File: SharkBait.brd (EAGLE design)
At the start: 50 x 92.4 mm, 37 parts, among them J1 BC501SM-TR, Q1 L78M05CDT, U2 DS3231M+

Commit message: brd version 1
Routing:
- net GND: track 378.1 -> 546.9 mm, vias 3 -> 8
- net A0: track 0.00 -> 114.6 mm, vias 0 -> 2
- net A1: track 0.00 -> 90.6 mm, vias 0 -> 1
- net 5V: track 190.3 -> 272.6 mm, vias 1 -> 5
- net D7: track 0.43 -> 76.5 mm, vias 0 -> 1
- net D4: track 0.00 -> 48.4 mm
- net RST: track 2.38 -> 30.7 mm, vias 0 -> 2
- net D5: track 34.1 -> 32.4 mm

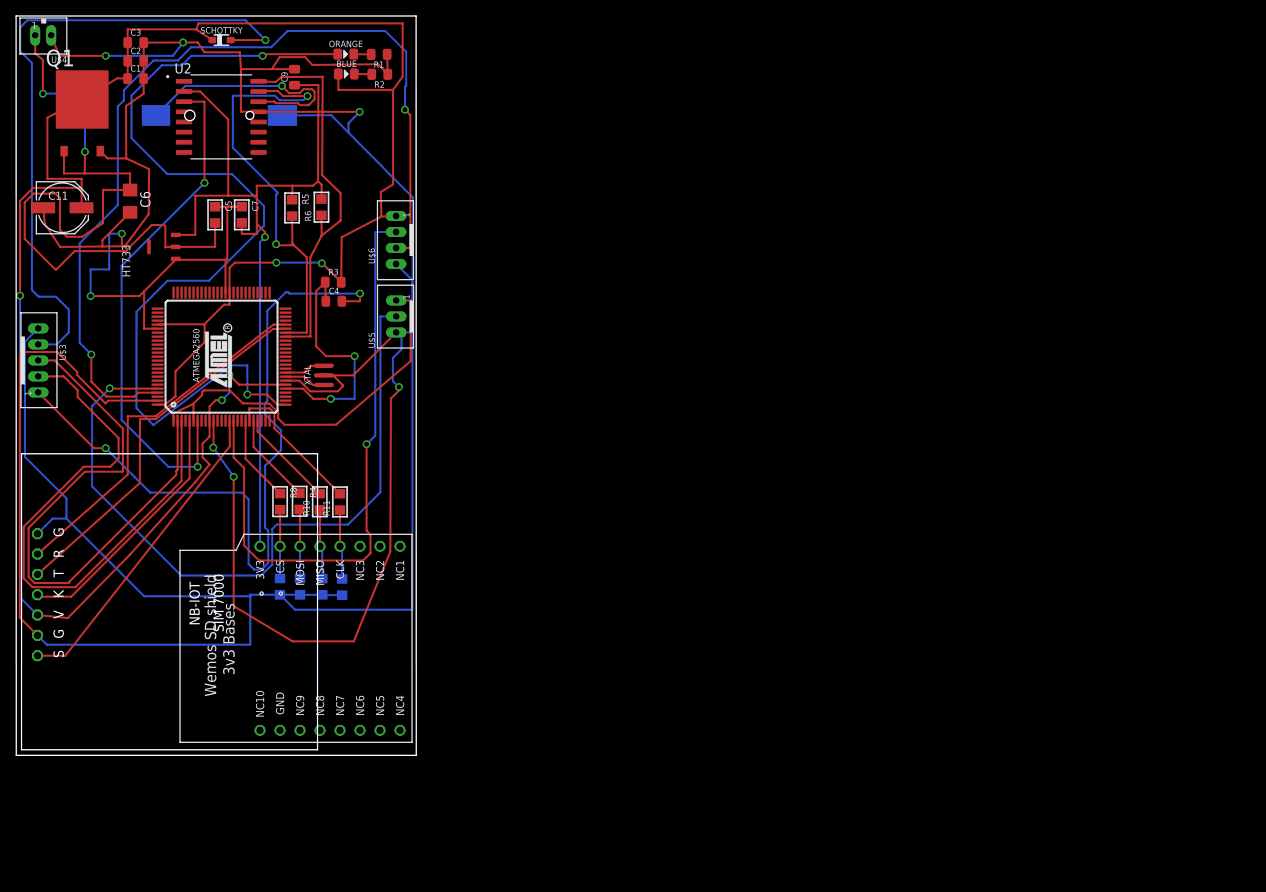
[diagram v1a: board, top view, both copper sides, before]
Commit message: revisi 3, termasuk pembetulan pin yang terbalik, dan regulator 5v yang terbalik
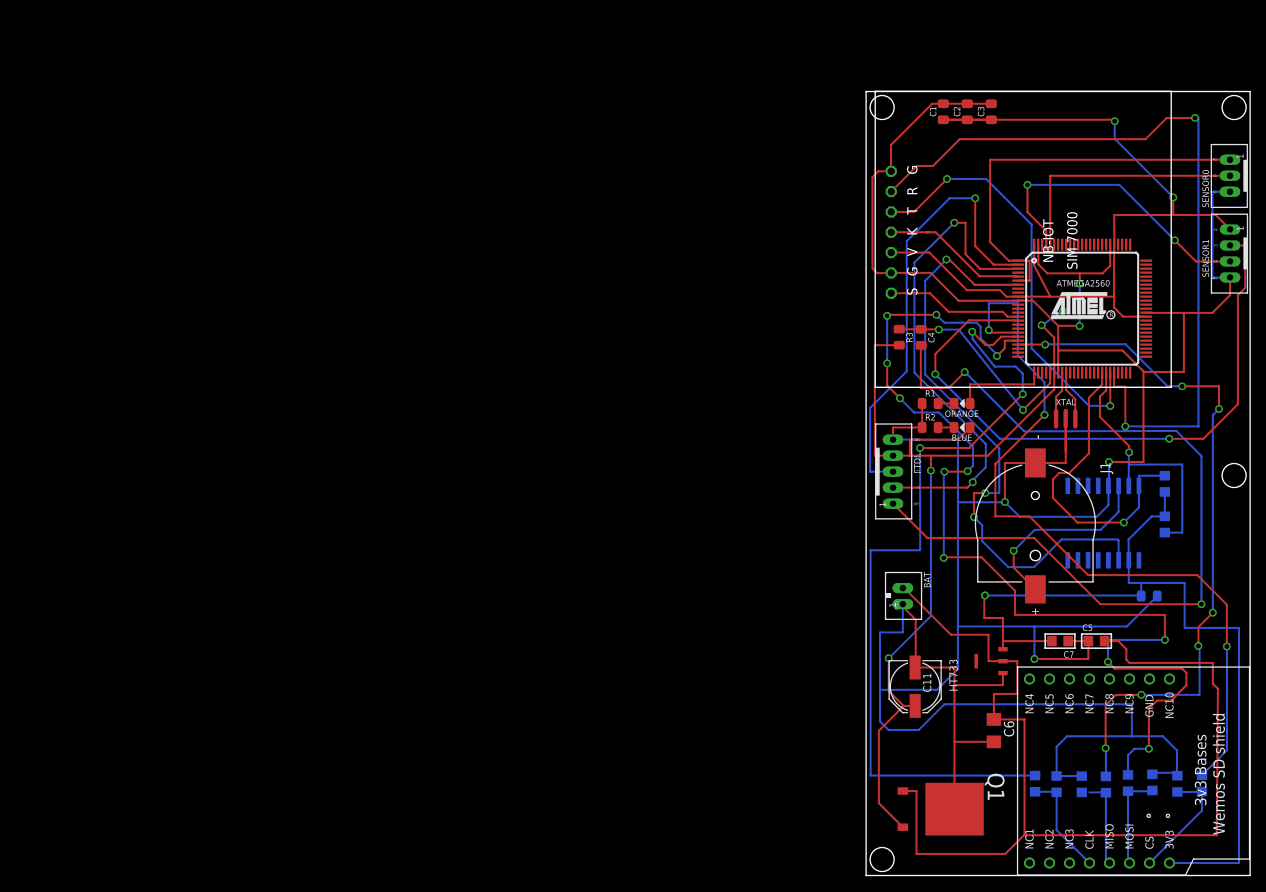
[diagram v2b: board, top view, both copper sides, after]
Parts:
- removed SCHOTTKY: DIODE, Fuzzy:SOD-323
- removed U$3: JST-PH_5-PIN_HEADER, srg:JST_B5B-PH_HEADER
- removed U$4: JST-PH_2-PIN_HEADER, srg:JST_B2B-PH_HEADER
- removed U$5: JST-PH_3-PIN_HEADER, srg:JST_B3B-PH_HEADER
- removed U$6: JST-PH_4-PIN_HEADER, srg:JST_B4B-PH_HEADER
- added BAT: JST-PH_2-PIN_HEADER, srg:JST_B2B-PH_HEADER
- added FTDI: JST-PH_5-PIN_HEADER, srg:JST_B5B-PH_HEADER
- added SENSOR0: JST-PH_3-PIN_HEADER, srg:JST_B3B-PH_HEADER
- added SENSOR1: JST-PH_4-PIN_HEADER, srg:JST_B4B-PH_HEADER
- moved Q1 140.4 mm to (10.9, 8.30), turned to 270 degrees
- moved U$1 140.3 mm to (47.9, 0.06), turned to 90 degrees
- moved C6 126.6 mm to (16.0, 18.1)
- moved C9 125.0 mm to (35.4, 34.9), flipped to the bottom, turned to 180 degrees
- moved C5 122.4 mm to (28.8, 29.3), turned to 0 degrees
- moved C11 122.3 mm to (6.13, 23.6), turned to 270 degrees
- moved U2 121.4 mm to (29.7, 44.0), flipped to the bottom, turned to 90 degrees
- moved R8 120.5 mm to (42.0, 11.5), flipped to the bottom
- moved R5 116.0 mm to (37.3, 43.9), flipped to the bottom
- moved U$2 115.9 mm to (1.14, 98.0)
- moved HT733 115.6 mm to (16.5, 26.8)
- moved C7 115.3 mm to (24.2, 29.3), turned to 180 degrees
- moved R9 114.8 mm to (38.9, 11.5), turned to 270 degrees
- moved J1 113.8 mm to (21.2, 44.0), flipped to the top, turned to 270 degrees
- moved R6 110.9 mm to (37.3, 49.0), flipped to the bottom, turned to 270 degrees
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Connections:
- removed net N$2: R4.2, R7.2, U$1.MISO
- removed net VCC: SCHOTTKY.A, U$3.P4
- new net N$3: R4.2, R7.2, U$1.MOSI
- net 5V: now also FTDI.P4, Q1.OUT, SENSOR1.P1; no longer Q1.2, SCHOTTKY.C, U$6.P1
- net A0: now also SENSOR1.P3; no longer U$6.P3
- net A1: now also SENSOR0.P2; no longer U$5.P2
- net D4: now also SENSOR0.P1; no longer U$5.P1
- net D7: now also SENSOR1.P2; no longer U$6.P2
- net DTR: now also FTDI.P1; no longer U$3.P1
- net GND: now also BAT.P1, FTDI.P5, Q1.GND, SENSOR0.P3, SENSOR1.P4; no longer Q1.3, U$3.P5, U$4.P2, U$5.P3, U$6.P4
- net MISO: now also U$1.MISO; no longer U$1.MOSI
- net RX0: now also FTDI.P3; no longer U$3.P3
- net TX0: now also FTDI.P2; no longer U$3.P2
- net VBAT: now also BAT.P2, Q1.IN; no longer Q1.1, U$4.P1
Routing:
- net MOSI: track 11.4 -> 134.2 mm, vias 0 -> 11
- net GND: track 546.9 -> 431.3 mm, vias 8 -> 5
- net D13: track 114.5 -> 11.9 mm, vias 2 -> 0
- net SCK: track 27.7 -> 115.3 mm, vias 0 -> 3
- net SS: track 10.9 -> 97.5 mm, vias 0 -> 3
- net VCC: track 82.8 -> 0.00 mm, vias 1 -> 0
- net MISO: track 21.1 -> 99.3 mm, vias 0 -> 7
- net A0: track 114.6 -> 37.7 mm
- net A1: track 90.6 -> 31.1 mm, vias 1 -> 0
- net TX1: track 46.0 -> 98.1 mm, vias 0 -> 2
- net 5V: track 272.6 -> 230.7 mm, vias 5 -> 6
- net VBAT: track 96.9 -> 133.9 mm, vias 2 -> 0
- net SDA: track 57.4 -> 33.4 mm, vias 2 -> 1
- net D6: track 40.0 -> 17.1 mm
- net DTR: track 92.4 -> 107.9 mm
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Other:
- board size 50 x 92.4 mm -> 48 x 98 mm
- board text added: "5V"
- board text added: "A0"
- board text added: "A1"
- board text added: "D4"
- board text added: "D7"
- board text added: "DTR"
- board text added: "GND"
- board text added: "Rx"
- board text added: "Tx"
